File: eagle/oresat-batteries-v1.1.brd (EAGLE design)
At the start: 94 x 93.5 mm, 62 parts, among them IC1 74AHC1G08DBV, U1 TCAN330, U2 STM32F042K6, X1 16MHz

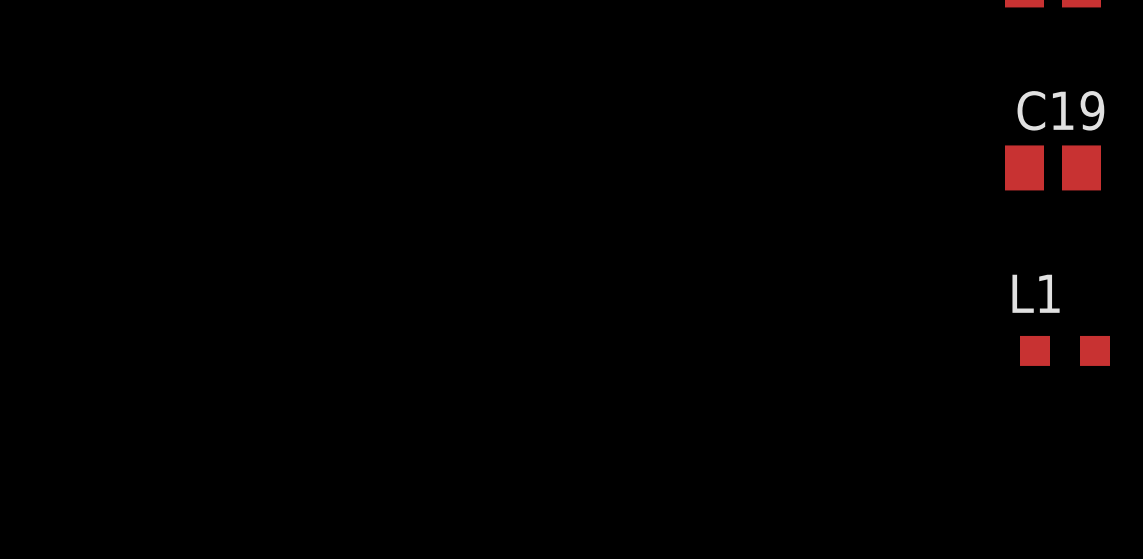
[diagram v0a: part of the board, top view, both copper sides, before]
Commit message: Added ideal diodes and new fuel gauge
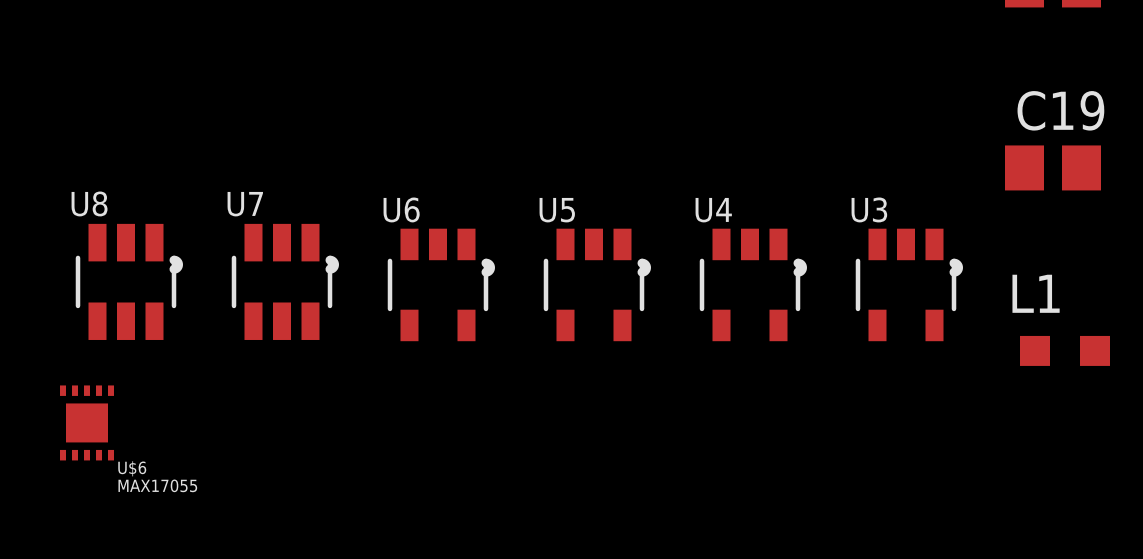
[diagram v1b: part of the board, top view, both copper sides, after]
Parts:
- added U$6: MAX17055, max17055:TDFN-10L
- added U3, U4, U5, U6: LTC4411, ltc4411:SOT23-5-B
- added U7, U8: LTC4412, ltc4412:SOT23-6
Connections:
- net GND: now also U3.2, U4.2, U5.2, U6.2, U7.2, U8.2
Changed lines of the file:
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@@
 <element name="C19" library="rcl" package="C0805" value="10u" x="-28.9" y="-92.6"/>
 <element name="L1" library="rcl" package="L2012C" value="" x="-28.5" y="-98.7"/>
+<element name="U3" library="ltc4411" package="SOT23-5-B" value="LTC4411" x="-33.8" y="-96.5"/>
+<element name="U4" library="ltc4411" package="SOT23-5-B" value="LTC4411" x="-39" y="-96.5"/>
+<element name="U5" library="ltc4411" package="SOT23-5-B" value="LTC4411" x="-44.2" y="-96.5"/>
+<element name="U6" library="ltc4411" package="SOT23-5-B" value="LTC4411" x="-49.4" y="-96.5"/>
+<element name="U7" library="ltc4412" package="SOT23-6" value="LTC4412" x="-54.6" y="-96.4"/>
+<element name="U8" library="ltc4412" package="SOT23-6" value="LTC4412" x="-59.8" y="-96.4"/>
+<element name="U$6" library="max17055" package="TDFN-10L" value="MAX17055" x="-61.1" y="-101.1"/>
 </elements>
 <signals>
@@
 <contactref element="U$1" pad="2"/>
 <contactref element="C17" pad="2"/>
+<contactref element="U3" pad="2"/>
+<contactref element="U4" pad="2"/>
+<contactref element="U5" pad="2"/>
+<contactref element="U6" pad="2"/>
+<contactref element="U7" pad="2"/>
+<contactref element="U8" pad="2"/>
+<wire x1="-54.6" y1="-95.09" x2="-59.8" y2="-95.09" width="0" layer="19" extent="1-1"/>
+<wire x1="-49.4" y1="-95.15" x2="-54.6" y2="-95.09" width="0" layer="19" extent="1-1"/>
+<wire x1="-44.2" y1="-95.15" x2="-49.4" y2="-95.15" width="0" layer="19" extent="1-1"/>
+<wire x1="-39" y1="-95.15" x2="-44.2" y2="-95.15" width="0" layer="19" extent="1-1"/>
+<wire x1="-33.8" y1="-95.15" x2="-39" y2="-95.15" width="0" layer="19" extent="1-1"/>
+<wire x1="-27.95" y1="-92.6" x2="-33.8" y2="-95.15" width="0" layer="19" extent="1-1"/>
 <wire x1="-27.95" y1="-86.5" x2="-27.95" y2="-92.6" width="0" layer="19" extent="1-1"/>
 <wire x1="-30.25" y1="-76.3" x2="-27.95" y2="-86.5" width="0" layer="19" extent="1-1"/>

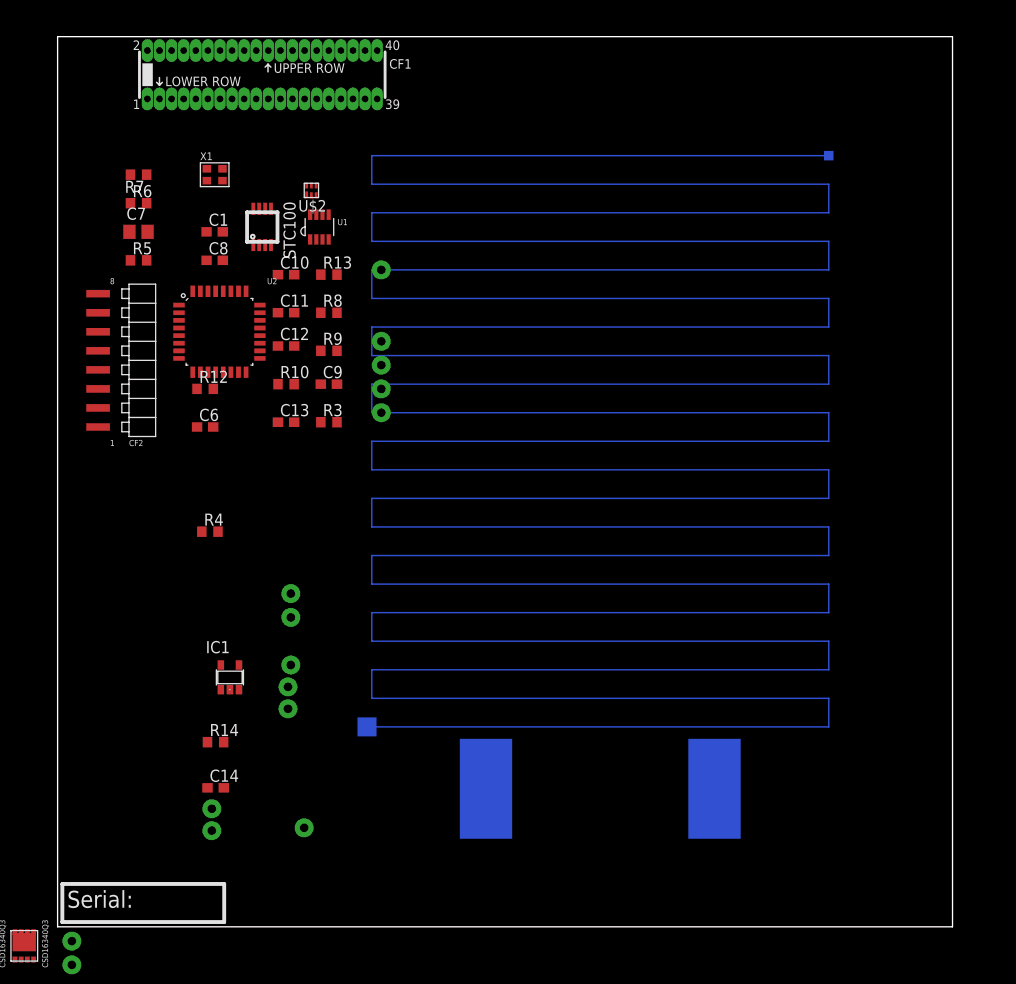
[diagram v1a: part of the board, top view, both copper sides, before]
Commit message: Updated batteries with latest OreSat card and connector.
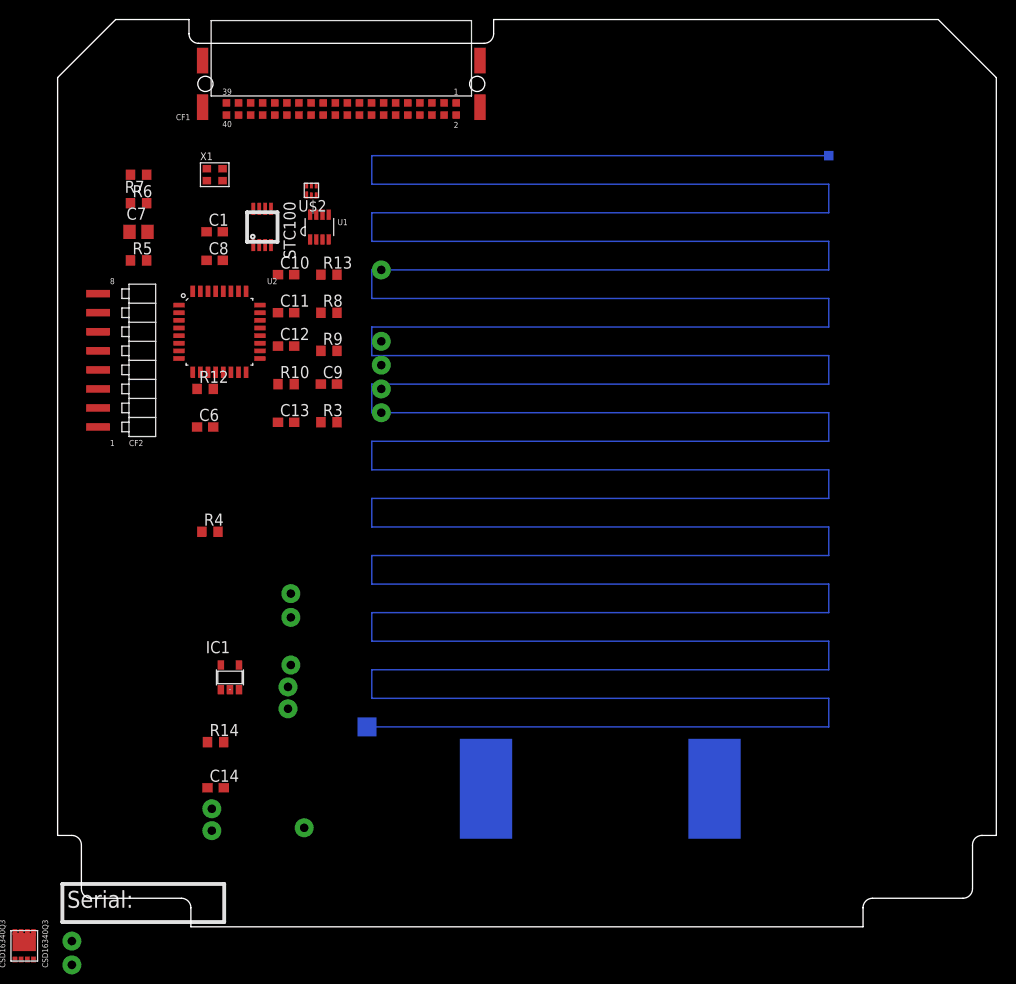
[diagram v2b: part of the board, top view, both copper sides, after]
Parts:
- added U$7: (no value), oresat-eagle:ORESAT-CARD-V0.5
- CF1: value ORESAT-CONNECTOR-40PIN -> CON-HARTING-FLEX-M-RA-1.27-1515040X601XXX; device low-gain-radio:HARWIN-ARCHER-M50-3202045 -> oresat-eagle:CON-1.27-M-RA-HARTING-1515040X601XXX
- moved CF1 8.36 mm to (29.8, 88.5), turned to 180 degrees
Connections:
- net BATOUT: now also CF1.3; no longer CF1.P$3
- net BQBAT: now also CF1.6; no longer CF1.P$6
- net CANH: now also CF1.2; no longer CF1.P$2
- net CANL: now also CF1.1; no longer CF1.P$1
- net VSOLAR: now also CF1.4; no longer CF1.P$4
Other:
- board size 94 x 93.5 mm -> 98.6 x 95.3 mm
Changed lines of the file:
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@@
 <?xml version="1.0" encoding="utf-8"?>
 <!DOCTYPE eagle SYSTEM "eagle.dtd">
-<eagle version="7.5.0">
+<eagle version="7.7.0">
 <drawing>
 <settings>
@@
 <layer number="2" name="Route2" color="1" fill="3" visible="no" active="no"/>
 <layer number="3" name="Route3" color="4" fill="3" visible="no" active="no"/>
+<layer number="4" name="Route4" color="1" fill="4" visible="yes" active="yes"/>
+<layer number="5" name="Route5" color="4" fill="4" visible="yes" active="yes"/>
+<layer number="6" name="Route6" color="1" fill="8" visible="yes" active="yes"/>
+<layer number="7" name="Route7" color="4" fill="8" visible="yes" active="yes"/>
+<layer number="8" name="Route8" color="1" fill="2" visible="yes" active="yes"/>
+<layer number="9" name="Route9" color="4" fill="2" visible="yes" active="yes"/>
+<layer number="10" name="Route10" color="1" fill="7" visible="yes" active="yes"/>
+<layer number="11" name="Route11" color="4" fill="7" visible="yes" active="yes"/>
+<layer number="12" name="Route12" color="1" fill="5" visible="yes" active="yes"/>
+<layer number="13" name="Route13" color="4" fill="5" visible="yes" active="yes"/>
 <layer number="14" name="Route14" color="1" fill="6" visible="no" active="no"/>
 <layer number="15" name="Route15" color="4" fill="6" visible="no" active="no"/>
@@
 <board>
 <plain>
-<wire x1="0" y1="0" x2="94" y2="0" width="0" layer="20"/>
-<wire x1="94" y1="0" x2="94" y2="93.5" width="0" layer="20"/>
-<wire x1="94" y1="93.5" x2="0" y2="93.5" width="0" layer="20"/>
-<wire x1="0" y1="93.5" x2="0" y2="0" width="0" layer="20"/>
 <wire x1="0.5" y1="0.5" x2="0.5" y2="4.5" width="0.4064" layer="25"/>
 <wire x1="0.5" y1="4.5" x2="17.5" y2="4.5" width="0.4064" layer="25"/>
@@
 <element name="U$2" library="oresat-batteries" package="PSOP6" value="BQ2970" x="26.66" y="77.35"/>
 <element name="U1" library="oresat-batteries" package="SOT23-8_TI-DCN" value="TCAN330" x="27.5" y="73.5"/>
-<element name="CF1" library="low-gain-radio" package="HARWIN-ARCHER-M50-3202045" value="ORESAT-CONNECTOR-40PIN" x="21.5" y="89.5"/>
+<element name="CF1" library="oresat-eagle" package="CON-1.27-M-RA-HARTING-1515040X601XXX" value="CON-HARTING-FLEX-M-RA-1.27-1515040X601XXX" x="29.8" y="88.54" locked="yes" rot="R180"/>
 <element name="U$5" library="oresat-batteries" package="MINISO-8" value="STC3100LST" x="21.5" y="73.5"/>
 <element name="C1" library="rcl" package="C0603" value=".1u" x="16.5" y="73"/>
@@
 <element name="U8" library="ltc4412" package="SOT23-6" value="LTC4412" x="-59.8" y="-96.4"/>
 <element name="U$6" library="max17055" package="TDFN-10L" value="MAX17055" x="-61.1" y="-101.1"/>
+<element name="U$7" library="oresat-eagle" package="ORESAT-CARD-V0.5" value="" x="0" y="0" locked="yes"/>
 </elements>
 <signals>
@@
 <contactref element="DEBUG_DNP" pad="7"/>
 <contactref element="DEBUG_DNP" pad="8"/>
-<contactref element="CF1" pad="P$4"/>
-<wire x1="0.23" y1="-13.73" x2="10.705" y2="92.04" width="0" layer="19" extent="1-1"/>
+<contactref element="CF1" pad="4"/>
+<wire x1="0.23" y1="-13.73" x2="40.595" y2="85.27" width="0" layer="19" extent="1-1"/>
 <wire x1="0.23" y1="-16.27" x2="0.23" y2="-13.73" width="0" layer="19" extent="1-1"/>
 </signal>
@@
 <contactref element="IC1" pad="1"/>
 <contactref element="R14" pad="2"/>
-<contactref element="CF1" pad="P$6"/>
+<contactref element="CF1" pad="6"/>
 <contactref element="U$4" pad="P$1"/>
 <contactref element="U$26" pad="P$1"/>
@@
 <wire x1="15.65" y1="73" x2="26.66" y2="77.875" width="0" layer="19" extent="1-1"/>
 <wire x1="9.35" y1="79" x2="15.65" y2="73" width="0" layer="19" extent="1-1"/>
-<wire x1="11.975" y1="92.04" x2="9.35" y2="79" width="0" layer="19" extent="1-1"/>
+<wire x1="39.325" y1="85.27" x2="9.35" y2="79" width="0" layer="19" extent="1-1"/>
 <wire x1="24.2" y1="25.2" x2="15.65" y2="73" width="0" layer="19" extent="1-1"/>
 <wire x1="17.15" y1="24.91" x2="24.2" y2="25.2" width="0" layer="19" extent="1-1"/>
@@
 <contactref element="DEBUG_DNP" pad="14"/>
 <contactref element="DEBUG_DNP" pad="13"/>
-<contactref element="CF1" pad="P$2"/>
+<contactref element="CF1" pad="2"/>
 <contactref element="U$12" pad="P$1"/>
-<wire x1="9.435" y1="92.04" x2="27.175" y2="74.8" width="0" layer="19" extent="1-1"/>
+<wire x1="41.865" y1="85.27" x2="27.175" y2="74.8" width="0" layer="19" extent="1-1"/>
 <wire x1="1.5" y1="-4" x2="27.175" y2="74.8" width="0" layer="19" extent="1-1"/>
 <wire x1="7.85" y1="-13.73" x2="1.5" y2="-4" width="0" layer="19" extent="1-1"/>
@@
 <contactref element="DEBUG_DNP" pad="12"/>
 <contactref element="DEBUG_DNP" pad="11"/>
-<contactref element="CF1" pad="P$1"/>
+<contactref element="CF1" pad="1"/>
 <contactref element="U$8" pad="P$1"/>
-<wire x1="9.435" y1="86.96" x2="27.825" y2="74.8" width="0" layer="19" extent="1-1"/>
+<wire x1="41.865" y1="86.54" x2="27.825" y2="74.8" width="0" layer="19" extent="1-1"/>
 <wire x1="1.5" y1="-1.5" x2="27.825" y2="74.8" width="0" layer="19" extent="1-1"/>
 <wire x1="5.31" y1="-13.73" x2="1.5" y2="-1.5" width="0" layer="19" extent="1-1"/>
@@
 </signal>
 <signal name="BATOUT">
-<contactref element="CF1" pad="P$3"/>
+<contactref element="CF1" pad="3"/>
 </signal>
 <signal name="3V3">

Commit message: Added 4412 and toshiba P-Channel Mosfets.
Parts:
- removed C6: .22u, rcl:C0603
- removed C7: 1u, rcl:C0805
- removed R4: 200k .1%, rcl:R0603
- removed R5: 1k, rcl:R0603
- added C2: .47u, rcl:C0603
- added C3: .1u, rcl:C0603
- added R1, R2: 10k, rcl:R0603
- added U$24, U$30: TPN4R712MD, tpn4r712md-pmosfet:TSON-ADVANCE-3X3
- added U10, U9: LTC4412, ltc4412:SOT23-6
- U$29: value TP -> TPN4R712MD; device oresat-batteries:2MM_TP -> tpn4r712md-pmosfet:TSON-ADVANCE-3X3
- U$5: value STC3100LST -> TPN4R712MD; device oresat-batteries:MINISO-8 -> tpn4r712md-pmosfet:TSON-ADVANCE-3X3
- moved U$5 216.4 mm to (-75.7, -119.8)
- moved U$29 133.9 mm to (-75.7, -146.1)
- moved U8 46.2 mm to (-76.3, -139.6)
- moved U7 37.1 mm to (-76.3, -126.5)
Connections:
- removed net IO0: R10.1, R13.2, U$5.1, U$9.P$1
- removed net ROSC: R4.2, U$5.2
- removed net STC_CG: U$14.P$1, U$14.P$2, U$14.P$3, U$2.4, U$3.NEG
- removed net STC_VIN: C6.2, R5.1, U$5.8
- new net 4411MB: U5.5, U6.1
- new net 4411_MT: U3.5, U4.1
- new net ALERT: R10.1, R13.2, U$6.8, U$9.P$1
- new net BATT+: C15.1, C16.1, C3.1, R21.2, R7.2, U$1.1, U$24.5, U$24.6, U$24.7, U$24.8, U$3.POS, U$30.5, U$30.6, U$30.7, U$30.8, U$6.10, U4.5, U6.5, U7.1, U9.1
- new net BATT-: R2.1, U$14.P$1, U$14.P$2, U$14.P$3, U$2.4, U$3.NEG
- new net CHG_SHD: U3.3, U4.3, U5.3, U6.3
- new net DSCHG_SHD: U10.3, U7.3, U8.3, U9.3
- new net N$11: U$24.1, U$24.2, U$24.3, U$5.5, U$5.6, U$5.7, U$5.8, U10.1, U7.6
- new net N$12: U$24.4, U7.5
- new net N$16: U$29.4, U8.5
- new net N$18: U$29.5, U$29.6, U$29.7, U$29.8, U$30.1, U$30.2, U$30.3, U8.1, U9.6
- new net N$19: U$30.4, U9.5
- new net N$8: U$5.4, U10.5
- new net REG: C2.1, U$6.7
- new net THRM: R1.2, U$6.9
- new net VBATT: U$29.1, U$29.2, U$29.3, U$5.1, U$5.2, U$5.3, U10.6, U8.6
- net C_SENSE: now also U$6.6; no longer U$5.6
- net GND: now also C2.2, C3.2, U$6.5, U10.2, U9.2; no longer C6.1, C7.1, R4.1, U$5.5
- net N$3: now also R1.1, R2.2, U$6.2; no longer C15.1, C16.1, C7.2, R21.2, R5.2, R7.2, U$1.1, U$29.P$1, U$3.POS, U$5.7
- net SCL: now also U$6.3; no longer U$5.4
- net SDA: now also U$6.4; no longer U$5.3
- net VSOLAR: now also U3.1, U5.1

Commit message: Added charge and discharge control, lowside shutdown, test points and finished rough v1.1 design.
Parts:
- added R11, R15, R16, R17, R18, R23, R4, R5: 470k, rcl:R0603
- added R19, R22: 10k, rcl:R0603
- added U$31: MC74HC1G04DFT1GOSCT, MC74HC1G04DFT1GOSCT:SC70-5
- added U$32, U$33, U$34, U$35, U$36, U$37, U$38, U$39, U$40, U$41, U$42, U$43, U$44, U$45, U$46, U$47, U$48, U$49, U$50: TP, oresat-batteries:2MM_TP
- U$27: value TP -> MC74HC1G04DFT1GOSCT; device oresat-batteries:2MM_TP -> MC74HC1G04DFT1GOSCT:SC70-5
- moved U$27 243.4 mm to (-75.7, -199.0)
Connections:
- removed net BATOUT: CF1.3
- removed net BQBAT: C1.1, CF1.6, IC1.1, R14.2, R7.1, U$2.5, U$26.P$1, U$4.P$1
- removed net PA8: U$27.P$1, U2.18
- removed net SYS_EN: U2.14
- removed net VBATT: U$29.1, U$29.2, U$29.3, U$5.1, U$5.2, U$5.3, U10.6, U8.6
- removed net VBATT+: CF2.2
- new net CHG_CTL: CF1.7, R22.1, U$27.2
- new net DCHG_CTL: CF1.9, R19.1, U$31.2
- new net LOWSHD: C1.1, CF1.11, IC1.1, R14.2, R7.1, U$2.5, U$26.P$1, U$4.P$1
- new net U10STAT: R5.2, U10.4, U2.26
- new net U3STAT: R23.2, U2.18, U3.4
- new net U4STAT: R17.2, U2.12, U4.4
- new net U5STAT: R18.2, U2.13, U5.4
- new net U6STAT: R16.2, U2.11, U6.4
- new net U7STAT: R15.2, U2.10, U7.4
- new net U8STAT: R4.2, U2.27, U8.4
- new net U9STAT: R11.2, U2.15, U9.4
- net 3V3: now also CF2.2, R11.1, R15.1, R16.1, R17.1, R18.1, R23.1, R4.1, R5.1, U$38.P$1, U$39.P$1
- net BATT+: now also R19.2, R22.2, U$27.3, U$31.3, U$50.P$1
- net CANH: now also U$42.P$1
- net CANL: now also U$43.P$1
- net CHG_SHD: now also U$27.4, U$47.P$1, U$48.P$1
- net DSCHG_SHD: now also U$31.4, U$46.P$1
- net GND: now also U$27.5, U$31.5
- net NRESET: now also U$37.P$1
- net SCL: now also R8.1; no longer R9.1
- net SDA: now also R9.1; no longer R8.1
- net STM_DEBUG: now also U$32.P$1
- net SWCLK: now also U$36.P$1
- net SWDIO: now also U$35.P$1
- net USART2_RX: now also U$33.P$1, U$41.P$1, U$44.P$1
- net USART2_TX: now also U$34.P$1, U$40.P$1
- net VSOLAR: now also CF1.3, CF1.5, CF1.6, DEBUG_DNP.10, DEBUG_DNP.9, U$29.1, U$29.2, U$29.3, U$45.P$1, U$49.P$1, U$5.1, U$5.2, U$5.3, U10.6, U8.6
